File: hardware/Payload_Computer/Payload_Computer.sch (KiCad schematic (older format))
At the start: 0 parts

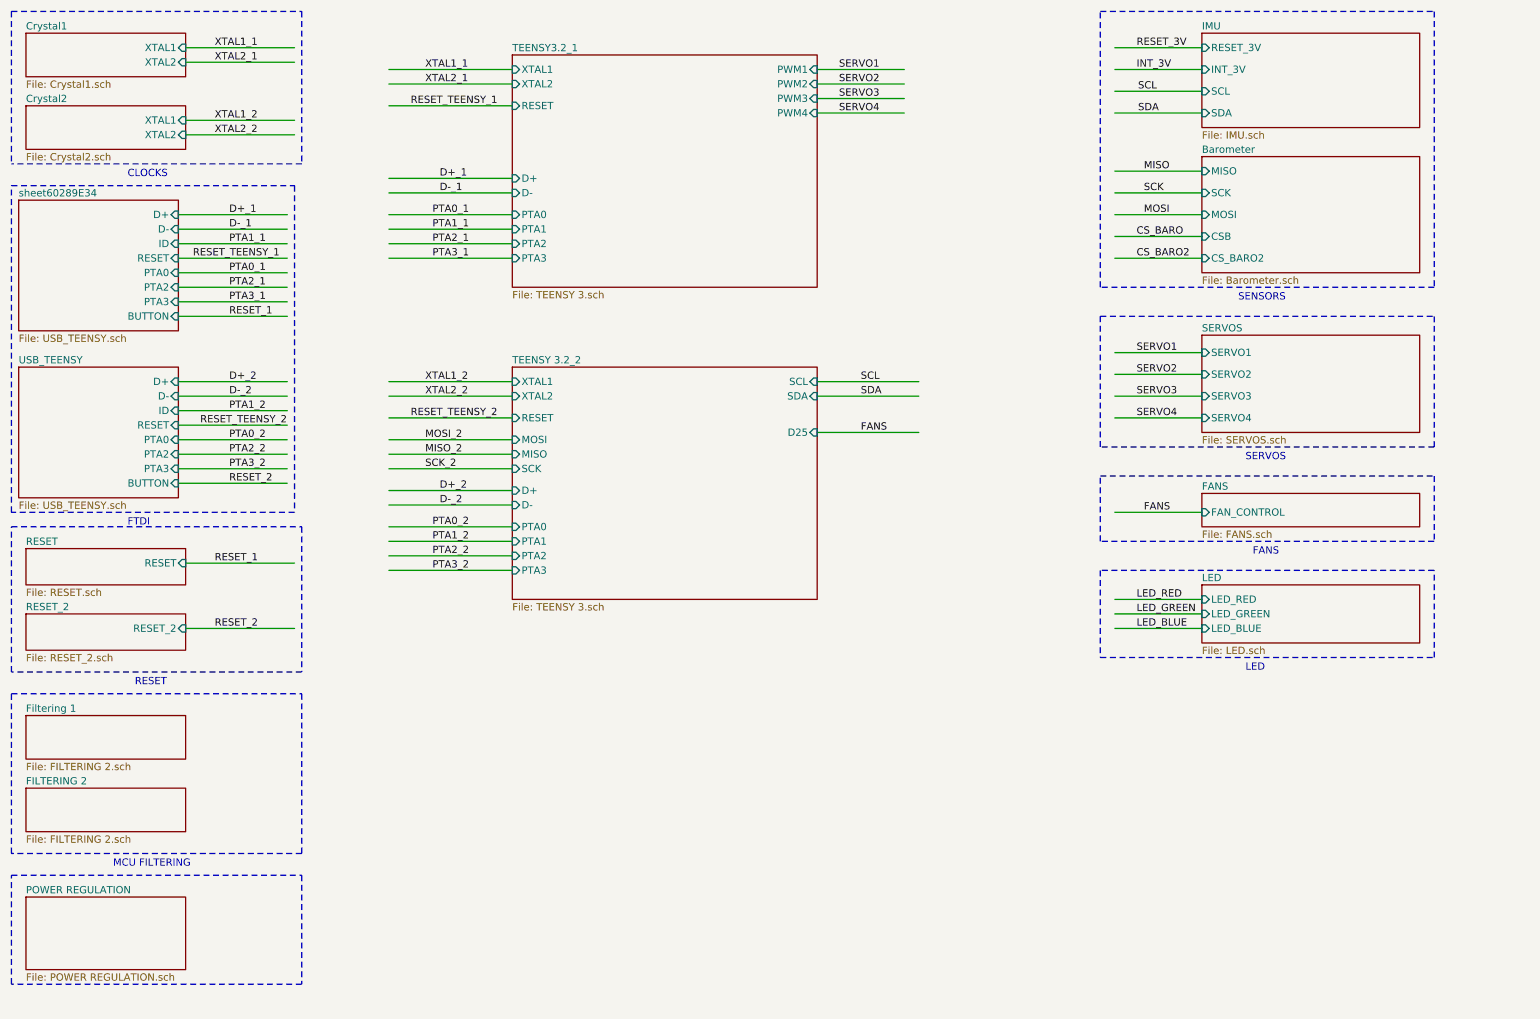
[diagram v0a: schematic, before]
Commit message: Added SD card and Battery Connector
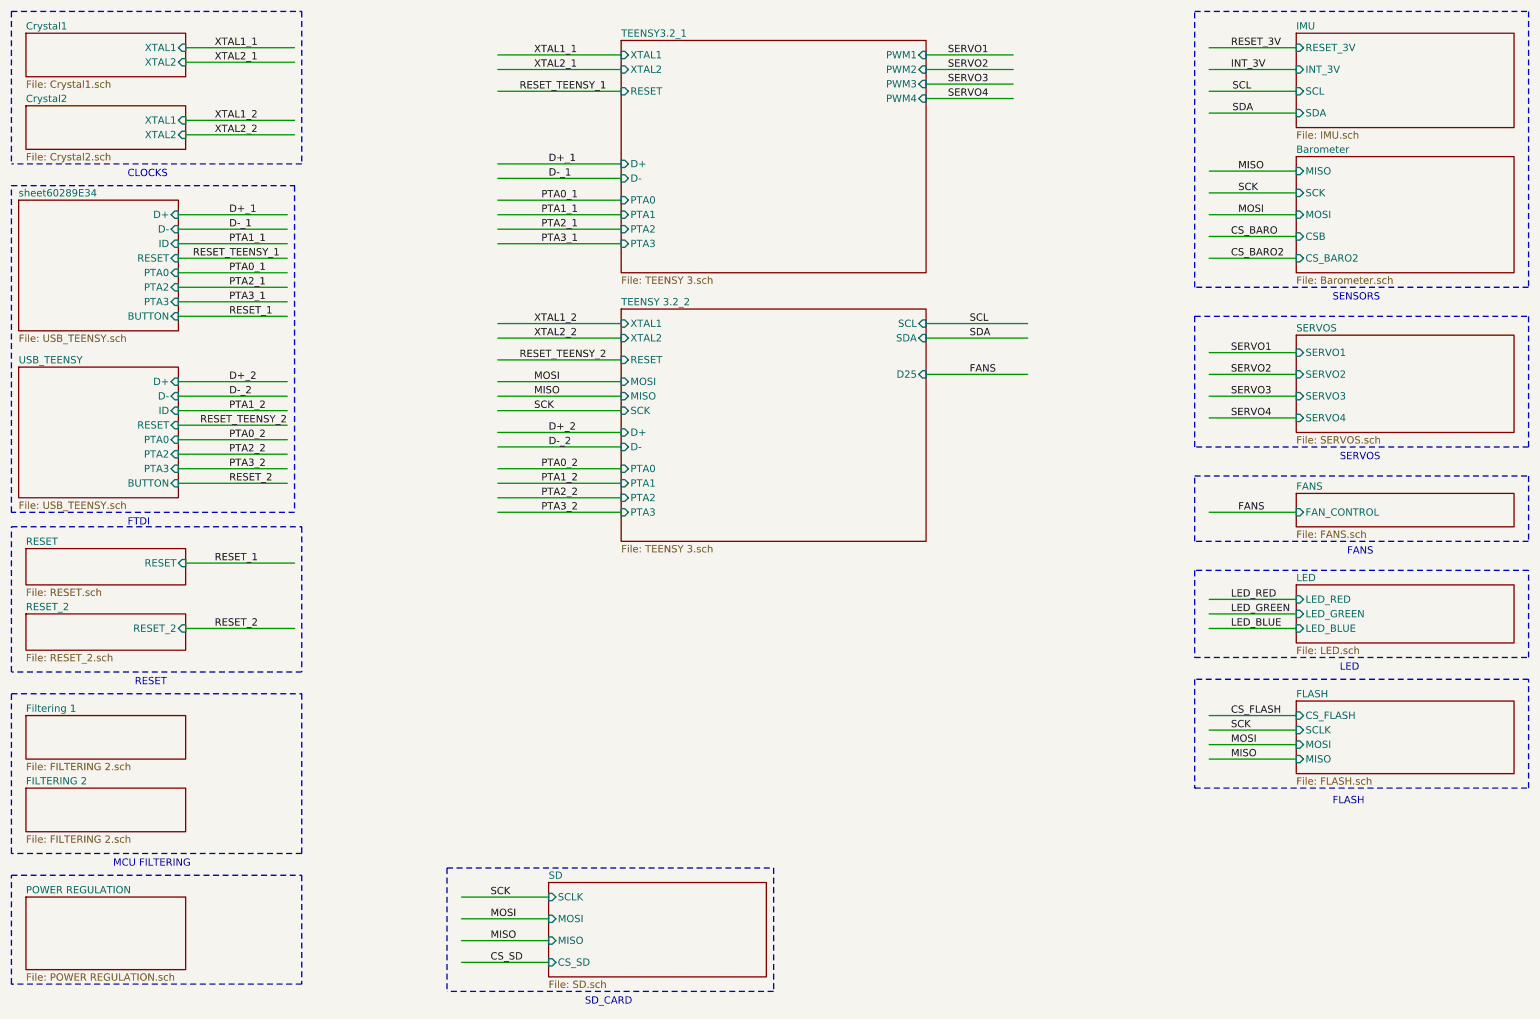
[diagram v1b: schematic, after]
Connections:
- net labels added: CS_FLASH, CS_SD
- net labels removed: MISO_2, MOSI_2, SCK_2
- wire segments 67 -> 75
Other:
- note added: "FLASH\n\n"
- note added: "SD_CARD\n"

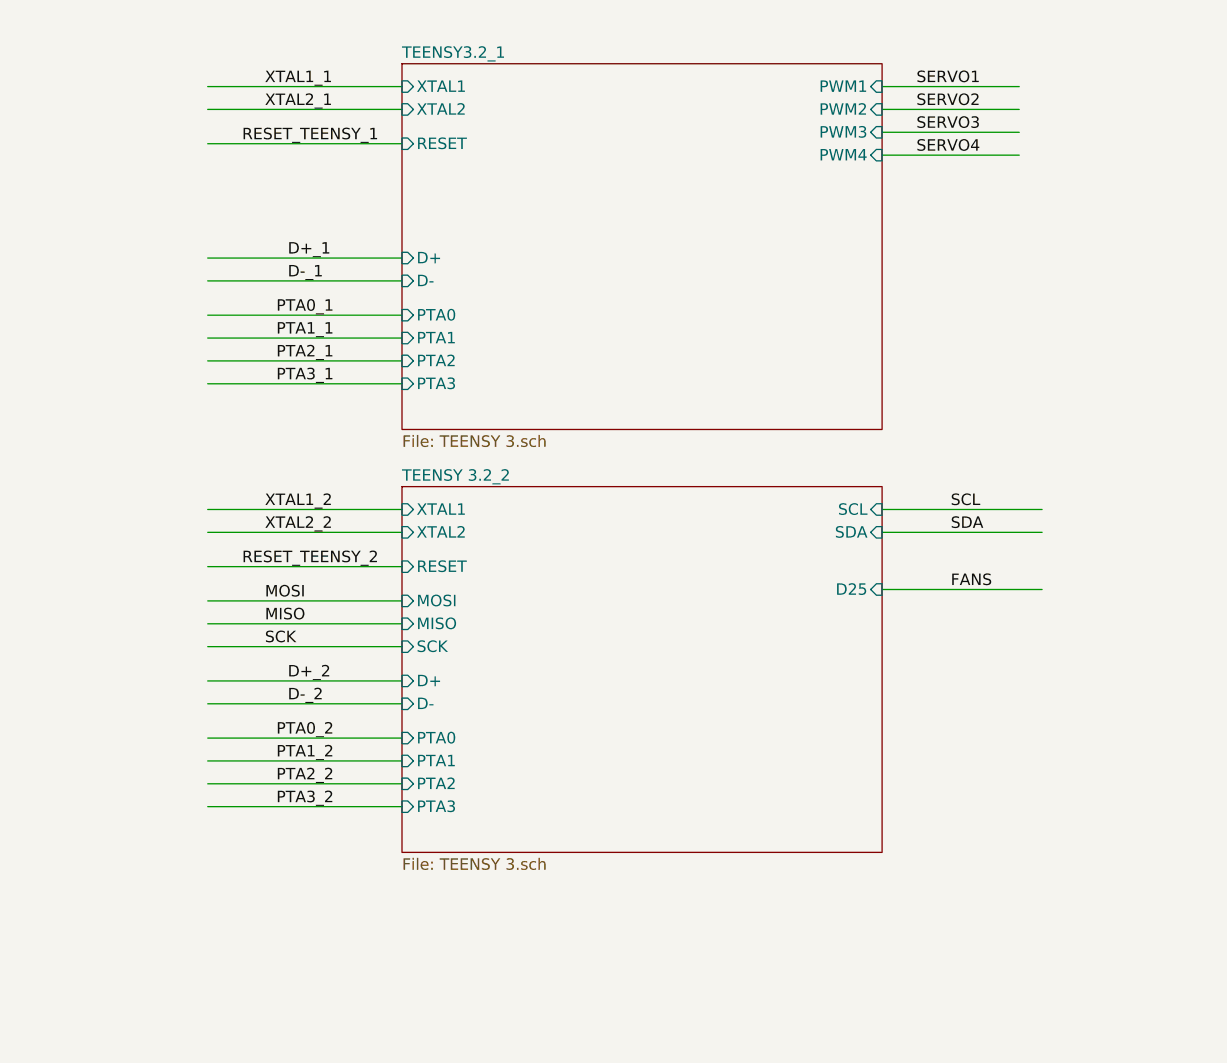
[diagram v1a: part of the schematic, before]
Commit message: Added last footprints and started routing
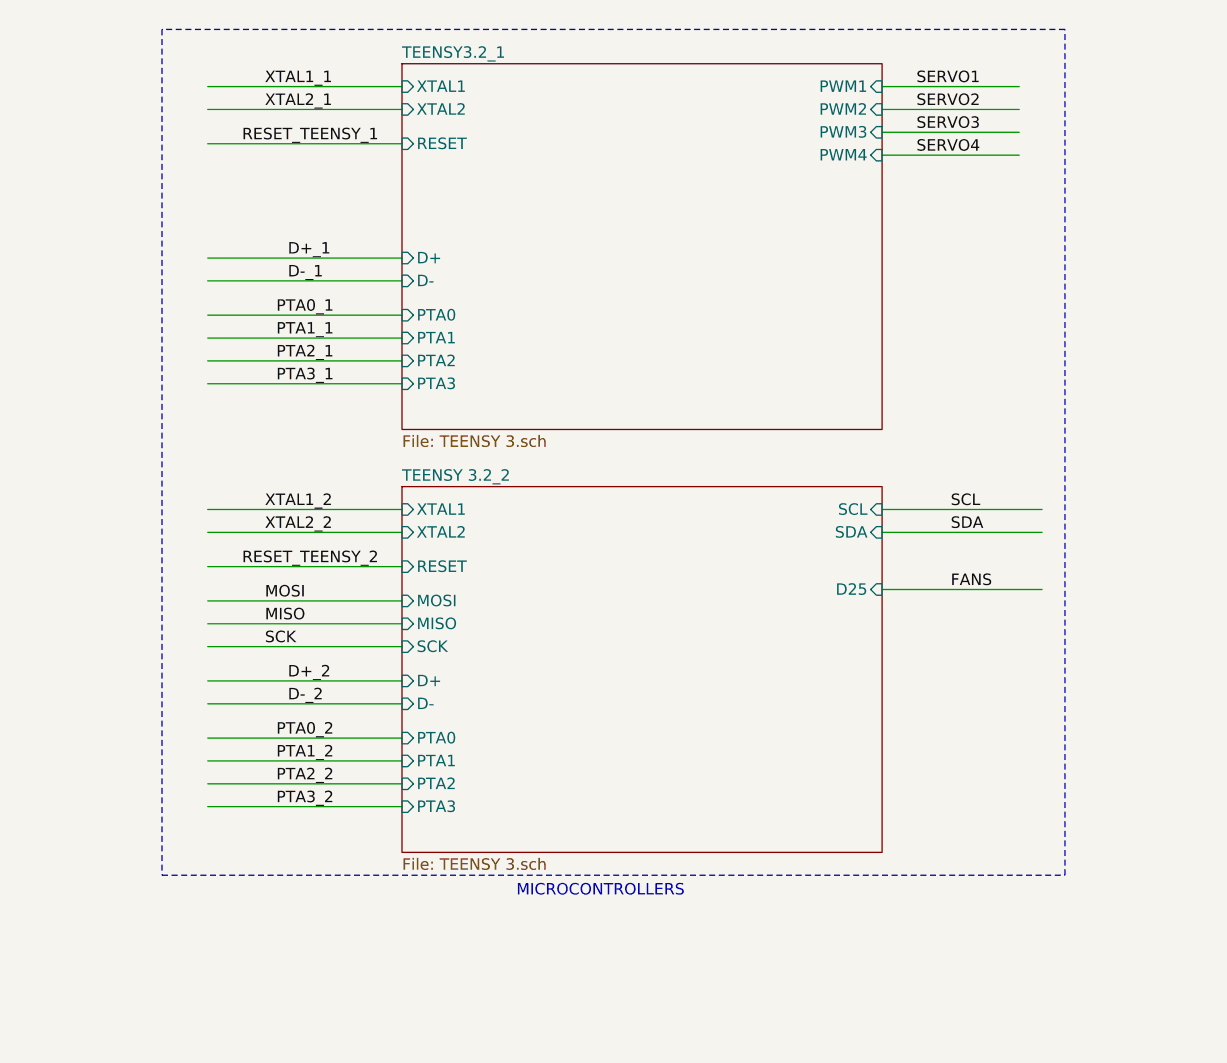
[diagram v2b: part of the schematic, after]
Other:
- note added: "MICROCONTROLLERS\n"
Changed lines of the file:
@@
 Text Notes 4600 7400 0    50   ~ 0
 SD_CARD\n
+Wire Notes Line
+	3800 600  3800 4300
+Wire Notes Line
+	3800 4300 7750 4300
+Wire Notes Line
+	7750 4300 7750 600
+Wire Notes Line
+	7750 600  3800 600
+Text Notes 5350 4400 0    50   ~ 0
+MICROCONTROLLERS\n
 $EndSCHEMATC

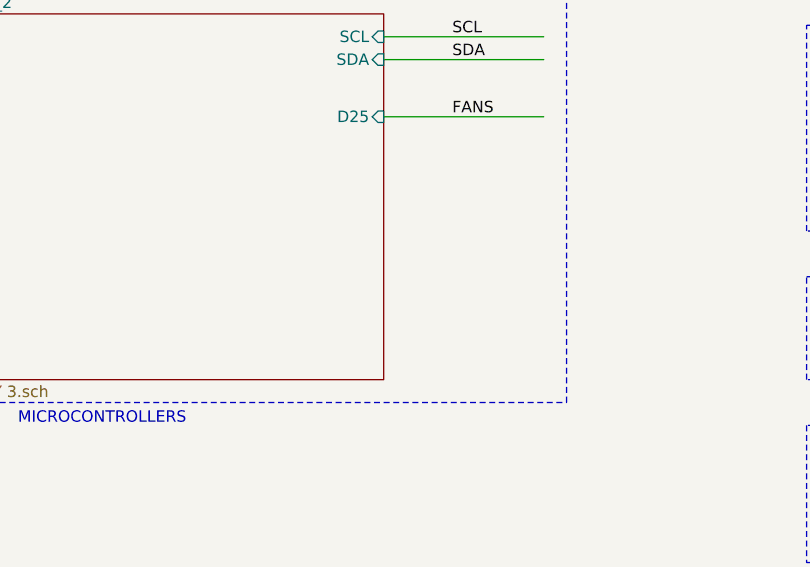
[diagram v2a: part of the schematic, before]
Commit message: Updated LED. Need to fix Mosfet footprint
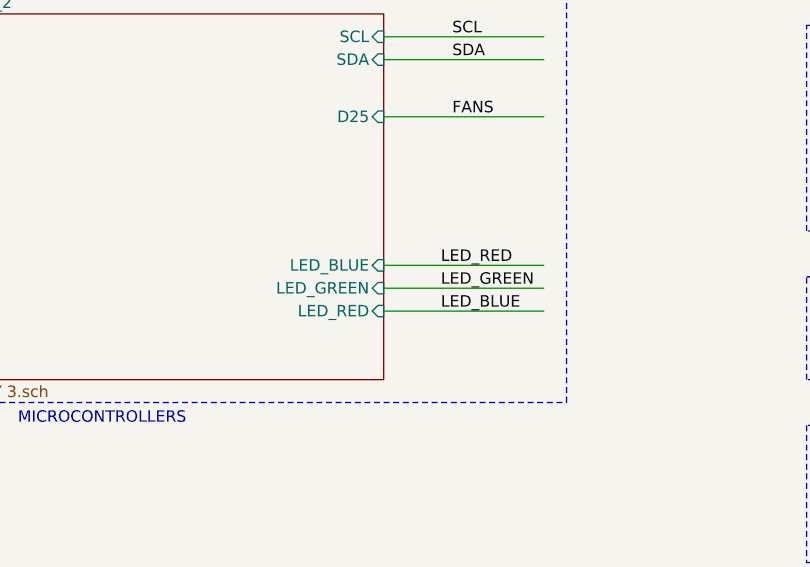
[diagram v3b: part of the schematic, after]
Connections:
- wire segments 75 -> 78
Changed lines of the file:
@@
 Wire Notes Line
 	8800 4200 8800 3750
-$Sheet
-S 4850 2600 2100 1600
-U 5F84585C
-F0 "TEENSY 3.2_2" 50
-F1 "TEENSY 3.sch" 50
-F2 "XTAL1" I L 4850 2700 50
-F3 "XTAL2" I L 4850 2800 50
-F4 "RESET" I L 4850 2950 50
-F5 "MOSI" I L 4850 3100 50
-F6 "MISO" I L 4850 3200 50
-F7 "SCK" I L 4850 3300 50
-F8 "D+" I L 4850 3450 50
-F9 "D-" I L 4850 3550 50
-F10 "PTA0" I L 4850 3700 50
-F11 "PTA1" I L 4850 3800 50
-F12 "PTA2" I L 4850 3900 50
-F13 "PTA3" I L 4850 4000 50
-F14 "SCL" I R 6950 2700 50
-F15 "SDA" I R 6950 2800 50
-F16 "D25" I R 6950 3050 50
-$EndSheet
 Wire Wire Line
 	6950 850  7550 850
@@
 Text Notes 5350 4400 0    50   ~ 0
 MICROCONTROLLERS\n
+$Sheet
+S 4850 2600 2100 1600
+U 5F84585C
+F0 "TEENSY 3.2_2" 50
+F1 "TEENSY 3.sch" 50
+F2 "XTAL1" I L 4850 2700 50
+F3 "XTAL2" I L 4850 2800 50
+F4 "RESET" I L 4850 2950 50
+F5 "MOSI" I L 4850 3100 50
+F6 "MISO" I L 4850 3200 50
+F7 "SCK" I L 4850 3300 50
+F8 "D+" I L 4850 3450 50
+F9 "D-" I L 4850 3550 50
+F10 "PTA0" I L 4850 3700 50
+F11 "PTA1" I L 4850 3800 50
+F12 "PTA2" I L 4850 3900 50
+F13 "PTA3" I L 4850 4000 50
+F14 "SCL" I R 6950 2700 50
+F15 "SDA" I R 6950 2800 50
+F16 "D25" I R 6950 3050 50
+F17 "LED_RED" I R 6950 3900 50
+F18 "LED_BLUE" I R 6950 3700 50
+F19 "LED_GREEN" I R 6950 3800 50
+$EndSheet
+Wire Wire Line
+	6950 3700 7650 3700
+Wire Wire Line
+	6950 3800 7650 3800
+Wire Wire Line
+	6950 3900 7650 3900
+Text Label 7200 3700 0    50   ~ 0
+LED_RED
+Text Label 7200 3800 0    50   ~ 0
+LED_GREEN
+Text Label 7200 3900 0    50   ~ 0
+LED_BLUE
 $EndSCHEMATC

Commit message: More Routing
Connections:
- net labels added: D1_+, D1_-, D2_+, D2_-
- net labels removed: D+_1, D+_2, D-_1, D-_2
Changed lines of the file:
@@
 	1800 3800 2550 3800
 Text Label 2150 3100 0    50   ~ 0
-D+_2
+D2_+
 Text Label 2150 3200 0    50   ~ 0
-D-_2
+D2_-
 Text Label 2150 3300 0    50   ~ 0
 PTA1_2
@@
 	4850 3700 4000 3700
 Text Label 4350 3450 0    50   ~ 0
-D+_2
+D2_+
 Text Label 4350 3550 0    50   ~ 0
-D-_2
+D2_-
 Wire Wire Line
 	4850 3800 4000 3800
@@
 	4850 1850 4000 1850
 Text Label 4350 1600 0    50   ~ 0
-D+_1
+D1_+
 Text Label 4350 1700 0    50   ~ 0
-D-_1
+D1_-
 Wire Wire Line
 	4850 1950 4000 1950
@@
 	1800 2650 2550 2650
 Text Label 2150 1950 0    50   ~ 0
-D+_1
+D1_+
 Text Label 2150 2050 0    50   ~ 0
-D-_1
+D1_-
 Text Label 2150 2150 0    50   ~ 0
 PTA1_1

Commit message: More Changes
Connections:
- net labels added: SERVO5, SERVO6
- wire segments 78 -> 84
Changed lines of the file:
@@
 $EndSheet
 $Sheet
-S 9500 2780 1500 670
+S 9500 2780 1500 920
 U 5FC5E24D
 F0 "SERVOS" 50
@@
 F4 "SERVO3" I L 9500 3200 50
 F5 "SERVO4" I L 9500 3350 50
-$EndSheet
-$Sheet
-S 9500 3870 1500 230
+F6 "SERVO5" I L 9500 3500 50
+F7 "SERVO6" I L 9500 3650 50
+$EndSheet
+$Sheet
+S 9500 4170 1500 230
 U 5FC6109B
 F0 "FANS" 50
 F1 "FANS.sch" 50
-F2 "FAN_CONTROL" I L 9500 4000 50
+F2 "FAN_CONTROL" I L 9500 4300 50
 $EndSheet
 Wire Wire Line
@@
 SERVO4
 Wire Notes Line
-	11100 2650 11100 3550
-Wire Notes Line
-	11100 3550 8800 3550
-Wire Notes Line
-	8800 3550 8800 2650
-Wire Notes Line
 	8800 2650 11100 2650
-Text Notes 9800 3650 0    50   ~ 0
+Text Notes 9800 3900 0    50   ~ 0
 SERVOS\n
 Wire Wire Line
-	9500 4000 8900 4000
-Wire Notes Line
-	8800 3750 11100 3750
-Wire Notes Line
-	11100 3750 11100 4200
-Wire Notes Line
-	11100 4200 8800 4200
-Wire Notes Line
-	8800 4200 8800 3750
+	9500 4300 8900 4300
+Wire Notes Line
+	8800 4050 11100 4050
+Wire Notes Line
+	11100 4050 11100 4500
+Wire Notes Line
+	11100 4500 8800 4500
+Wire Notes Line
+	8800 4500 8800 4050
 Wire Wire Line
 	6950 850  7550 850
@@
 Text Label 7250 3050 0    50   ~ 0
 FANS
-Text Label 9100 4000 0    50   ~ 0
+Text Label 9100 4300 0    50   ~ 0
 FANS
 $Sheet
@@
 $EndSheet
 $Sheet
-S 9500 4500 1500 400
+S 9500 4750 1500 400
 U 60334804
 F0 "LED" 50
 F1 "LED.sch" 50
-F2 "LED_RED" I L 9500 4600 50
-F3 "LED_GREEN" I L 9500 4700 50
-F4 "LED_BLUE" I L 9500 4800 50
-$EndSheet
-Wire Wire Line
-	9500 4600 8900 4600
-Wire Wire Line
-	9500 4700 8900 4700
-Wire Wire Line
-	9500 4800 8900 4800
-Text Label 9050 4600 0    50   ~ 0
+F2 "LED_RED" I L 9500 4850 50
+F3 "LED_GREEN" I L 9500 4950 50
+F4 "LED_BLUE" I L 9500 5050 50
+$EndSheet
+Wire Wire Line
+	9500 4850 8900 4850
+Wire Wire Line
+	9500 4950 8900 4950
+Wire Wire Line
+	9500 5050 8900 5050
+Text Label 9050 4850 0    50   ~ 0
 LED_RED
-Text Label 9050 4700 0    50   ~ 0
+Text Label 9050 4950 0    50   ~ 0
 LED_GREEN
-Text Label 9050 4800 0    50   ~ 0
+Text Label 9050 5050 0    50   ~ 0
 LED_BLUE
 Wire Notes Line
-	8800 5000 11100 5000
-Wire Notes Line
-	11100 5000 11100 4400
-Wire Notes Line
-	11100 4400 8800 4400
-Wire Notes Line
-	8800 4400 8800 5000
-Text Notes 9800 5100 0    50   ~ 0
+	8800 5250 11100 5250
+Wire Notes Line
+	11100 5250 11100 4650
+Wire Notes Line
+	11100 4650 8800 4650
+Wire Notes Line
+	8800 4650 8800 5250
+Text Notes 9800 5350 0    50   ~ 0
 LED\n
-Text Notes 9850 4300 0    50   ~ 0
+Text Notes 9850 4600 0    50   ~ 0
 FANS\n
 $Sheet
-S 9500 5300 1500 500
+S 9500 5550 1500 500
 U 60353E60
 F0 "FLASH" 50
 F1 "FLASH.sch" 50
-F2 "CS_FLASH" I L 9500 5400 50
-F3 "SCLK" I L 9500 5500 50
-F4 "MOSI" I L 9500 5600 50
-F5 "MISO" I L 9500 5700 50
-$EndSheet
-Wire Wire Line
-	9500 5400 8900 5400
-Wire Wire Line
-	9500 5500 8900 5500
-Wire Wire Line
-	9500 5600 8900 5600
-Wire Wire Line
-	9500 5700 8900 5700
-Text Label 9050 5400 0    50   ~ 0
+F2 "CS_FLASH" I L 9500 5650 50
+F3 "SCLK" I L 9500 5750 50
+F4 "MOSI" I L 9500 5850 50
+F5 "MISO" I L 9500 5950 50
+$EndSheet
+Wire Wire Line
+	9500 5650 8900 5650
+Wire Wire Line
+	9500 5750 8900 5750
+Wire Wire Line
+	9500 5850 8900 5850
+Wire Wire Line
+	9500 5950 8900 5950
+Text Label 9050 5650 0    50   ~ 0
 CS_FLASH
-Text Label 9050 5500 0    50   ~ 0
+Text Label 9050 5750 0    50   ~ 0
 SCK
-Text Label 9050 5600 0    50   ~ 0
+Text Label 9050 5850 0    50   ~ 0
 MOSI
-Text Label 9050 5700 0    50   ~ 0
+Text Label 9050 5950 0    50   ~ 0
 MISO
 Wire Notes Line
-	8800 5150 8800 5900
-Wire Notes Line
-	8800 5900 11100 5900
-Wire Notes Line
-	11100 5900 11100 5150
-Wire Notes Line
-	11100 5150 8800 5150
-Text Notes 9750 6100 0    50   ~ 0
+	8800 5400 8800 6150
+Wire Notes Line
+	8800 6150 11100 6150
+Wire Notes Line
+	11100 6150 11100 5400
+Wire Notes Line
+	11100 5400 8800 5400
+Text Notes 9750 6350 0    50   ~ 0
 FLASH\n\n
 $Sheet
@@
 F18 "LED_BLUE" I R 6950 3700 50
 F19 "LED_GREEN" I R 6950 3800 50
+F20 "PWM1" I R 6950 3200 50
+F21 "PWM2" I R 6950 3300 50
+F22 "PWM3" I R 6950 3400 50
+F23 "PWM4" I R 6950 3500 50
 $EndSheet
 Wire Wire Line
@@
 Text Label 7200 3900 0    50   ~ 0
 LED_BLUE
+Wire Wire Line
+	9500 3500 8900 3500
+Wire Wire Line
+	9500 3650 8900 3650
+Text Label 9050 3500 0    50   ~ 0
+SERVO5
+Text Label 9050 3650 0    50   ~ 0
+SERVO6
+Wire Notes Line
+	11100 3800 8800 3800
+Wire Notes Line
+	11100 2650 11100 3800
+Wire Notes Line
+	8800 2650 8800 3800
+Wire Wire Line
+	6950 3200 7650 3200
+Wire Wire Line
+	6950 3300 7650 3300
+Text Label 7200 3200 0    50   ~ 0
+SERVO5
+Text Label 7200 3300 0    50   ~ 0
+SERVO6
+Wire Wire Line
+	6950 3400 7650 3400
+Wire Wire Line
+	6950 3500 7650 3500
 $EndSCHEMATC
